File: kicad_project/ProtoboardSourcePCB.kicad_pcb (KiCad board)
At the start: 2 copper layers, 53 x 62.9 mm, 10 parts, among them J1 Conn_02x05_Odd_Even, J2 Conn_02x05_Odd_Even

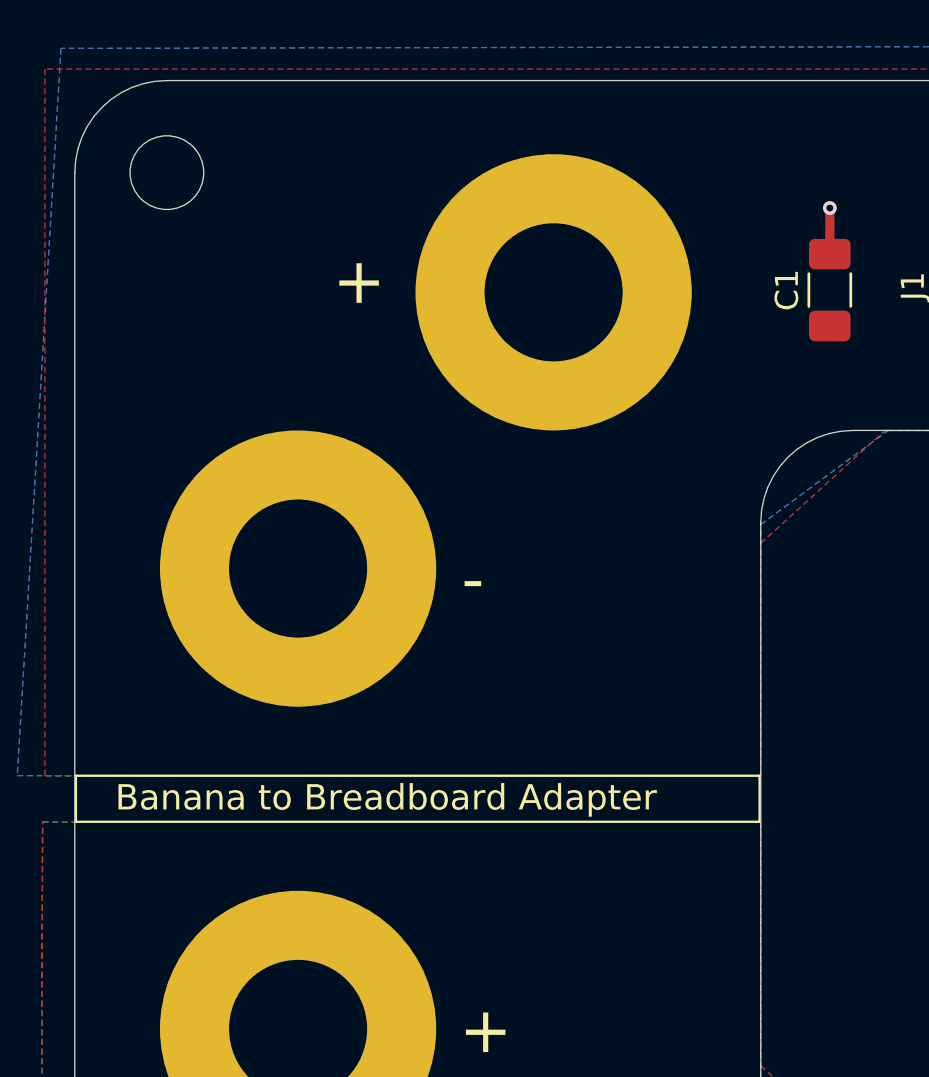
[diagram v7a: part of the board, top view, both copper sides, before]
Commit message: Agregando ultimos detalles y logo en el Silkscreen
Signed-off-by: RoMadrigal <rmadrigalmontes@gmail.com>
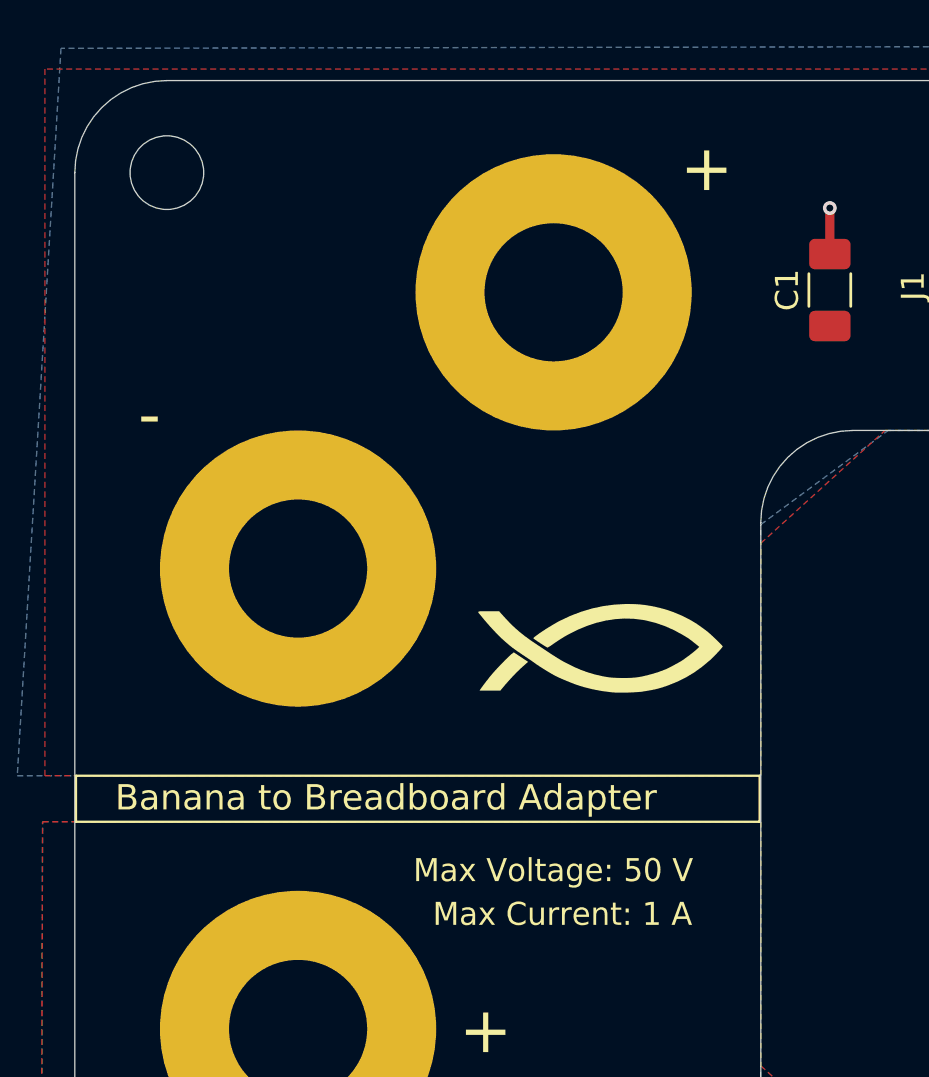
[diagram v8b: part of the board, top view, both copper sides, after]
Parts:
- added G***: LOGO, Logos:fish1, F.Cu at (133.0, 64.5)
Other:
- board text added: "Designed by: Rodrigo Madrigal Montes"
- board text added: "Max Current: 1 A"
- board text added: "Max Voltage: 50 V"
- board text removed: "Designed By: Rodrigo Madrigal Montes"
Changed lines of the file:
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@@
 	(net 3 "VDD")
 	(net 4 "GND2")
+	(footprint "Logos:fish1"
+		(layer "F.Cu")
+		(at 133 64.5)
+		(property "Reference" "G***"
+			(at 0 0 0)
+			(layer "F.SilkS")
+			(hide yes)
+			(effects
+				(font
+					(size 1.5 1.5)
+					(thickness 0.3)
+				)
+			)
+		)
+		(property "Value" "LOGO"
+			(at 0.75 0 0)
+			(layer "F.SilkS")
+			(hide yes)
+			(effects
+				(font
+					(size 1.5 1.5)
+					(thickness 0.3)
+				)
+			)
+		)
+		(property "Datasheet" ""
+			(at 0 0 0)
+			(layer "F.Fab")
+			(hide yes)
+			(effects
+				(font
+					(size 1.27 1.27)
+					(thickness 0.15)
+				)
+			)
+		)
+		(property "Description" ""
+			(at 0 0 0)
+			(layer "F.Fab")
+			(hide yes)
+			(effects
+				(font
+					(size 1.27 1.27)
+					(thickness 0.15)
+				)
+			)
+		)
+		(attr board_only exclude_from_pos_files exclude_from_bom)
+		(fp_poly
+			(pts
+				(xy -3.416751 0.347141) (xy -3.104273 0.554192) (xy -3.199105 0.633621) (xy -3.410967 0.821179)
+				(xy -3.633032 1.036653) (xy -3.858711 1.273265) (xy -4.081419 1.524236) (xy -4.189354 1.652689)
+				(xy -4.312394 1.801896) (xy -4.764901 1.801896) (xy -5.217408 1.801896) (xy -5.183151 1.748899)
+				(xy -5.132417 1.674759) (xy -5.06204 1.578084) (xy -4.977283 1.465756) (xy -4.883411 1.344657) (xy -4.785684 1.221668)
+				(xy -4.693054 1.108118) (xy -4.622083 1.025336) (xy -4.534365 0.927619) (xy -4.434648 0.819836)
+				(xy -4.327681 0.706856) (xy -4.218213 0.593549) (xy -4.110994 0.484784) (xy -4.010772 0.38543) (xy -3.922296 0.300357)
+				(xy -3.850316 0.234434) (xy -3.801413 0.193886) (xy -3.729229 0.14009)
+			)
+			(stroke
+				(width 0)
+				(type solid)
+			)
+			(fill yes)
+			(layer "F.SilkS")
+		)
+		(fp_poly
+			(pts
+				(xy 1.483303 -1.957004) (xy 1.731568 -1.942899) (xy 1.971119 -1.917313) (xy 2.214168 -1.878765)
+				(xy 2.472925 -1.825772) (xy 2.62814 -1.789502) (xy 2.947232 -1.699239) (xy 3.271495 -1.583108) (xy 3.591974 -1.445235)
+				(xy 3.899714 -1.289744) (xy 4.18576 -1.120761) (xy 4.400308 -0.973197) (xy 4.482943 -0.911861) (xy 4.574456 -0.843851)
+				(xy 4.65242 -0.785834) (xy 4.703224 -0.745084) (xy 4.770358 -0.687013) (xy 4.849201 -0.616058) (xy 4.93513 -0.536654)
+				(xy 5.023523 -0.453238) (xy 5.109757 -0.370247) (xy 5.189211 -0.292117) (xy 5.257261 -0.223283)
+				(xy 5.309286 -0.168183) (xy 5.340663 -0.131253) (xy 5.347875 -0.118368) (xy 5.334741 -0.092346)
+				(xy 5.298281 -0.044305) (xy 5.242906 0.021012) (xy 5.173027 0.098861) (xy 5.093055 0.1845) (xy 5.007401 0.273186)
+				(xy 4.920478 0.360174) (xy 4.836695 0.440723) (xy 4.776984 0.495474) (xy 4.444986 0.772471) (xy 4.107042 1.014674)
+				(xy 3.756826 1.225761) (xy 3.388009 1.409411) (xy 2.994261 1.569303) (xy 2.831818 1.626271) (xy 2.687166 1.672965)
+				(xy 2.550365 1.712411) (xy 2.412247 1.746695) (xy 2.263642 1.777904) (xy 2.095382 1.808123) (xy 1.898299 1.839439)
+				(xy 1.888618 1.840905) (xy 1.758321 1.856758) (xy 1.599572 1.869969) (xy 1.421535 1.880295) (xy 1.233372 1.887493)
+				(xy 1.044246 1.891316) (xy 0.863322 1.891522) (xy 0.699762 1.887866) (xy 0.562729 1.880104) (xy 0.529969 1.877122)
+				(xy 0.108151 1.822503) (xy -0.30112 1.745753) (xy -0.690215 1.6485) (xy -1.002125 1.549972) (xy -1.112419 1.509466)
+				(xy -1.243984 1.458203) (xy -1.387503 1.400087) (xy -1.533657 1.33902) (xy -1.67313 1.278904) (xy -1.796603 1.223644)
+				(xy -1.894759 1.177141) (xy -1.907892 1.170573) (xy -1.994925 1.123975) (xy -2.105421 1.060902)
+				(xy -2.230957 0.986533) (xy -2.363111 0.906046) (xy -2.493461 0.824622) (xy -2.613585 0.74744) (xy -2.71506 0.67968)
+				(xy -2.775115 0.637238) (xy -2.85329 0.581035) (xy -2.953241 0.511073) (xy -3.064443 0.434621) (xy -3.176368 0.358947)
+				(xy -3.227998 0.324544) (xy -3.402487 0.208179) (xy -3.550218 0.107616) (xy -3.677153 0.01829) (xy -3.789253 -0.06437)
+				(xy -3.892481 -0.144931) (xy -3.992797 -0.227962) (xy -4.096164 -0.31803) (xy -4.208544 -0.419704)
+				(xy -4.254558 -0.462062) (xy -4.363872 -0.567138) (xy -4.489643 -0.694826) (xy -4.62467 -0.83731)
+				(xy -4.761748 -0.986775) (xy -4.893676 -1.135406) (xy -5.013251 -1.275387) (xy -5.085056 -1.36318)
+				(xy -5.143797 -1.435812) (xy -5.194765 -1.49722) (xy -5.23271 -1.541189) (xy -5.252379 -1.561503)
+				(xy -5.252893 -1.561852) (xy -5.267907 -1.588241) (xy -5.27079 -1.610319) (xy -5.269218 -1.622191)
+				(xy -5.261441 -1.631246) (xy -5.242871 -1.637863) (xy -5.208916 -1.642424) (xy -5.154986 -1.64531)
+				(xy -5.076493 -1.646901) (xy -4.968845 -1.647579) (xy -4.827452 -1.647724) (xy -4.820149 -1.647725)
+				(xy -4.369509 -1.647725) (xy -4.296787 -1.56582) (xy -4.10984 -1.358811) (xy -3.936868 -1.17572)
+				(xy -3.771609 -1.011147) (xy -3.607807 -0.859692) (xy -3.439202 -0.715955) (xy -3.259537 -0.574533)
+				(xy -3.062551 -0.430027) (xy -2.841987 -0.277036) (xy -2.669121 -0.16128) (xy -2.471887 -0.030745)
+				(xy -2.303429 0.080565) (xy -2.160406 0.174738) (xy -2.039477 0.253863) (xy -1.937305 0.320027)
+				(xy -1.850547 0.375318) (xy -1.775865 0.421825) (xy -1.709918 0.461634) (xy -1.649367 0.496834)
+				(xy -1.590872 0.529514) (xy -1.531093 0.561759) (xy -1.466689 0.59566) (xy -1.416465 0.621805) (xy -1.103174 0.776125)
+				(xy -0.804527 0.904776) (xy -0.510074 1.011344) (xy -0.209365 1.099413) (xy 0.108052 1.172571) (xy 0.289073 1.206958)
+				(xy 0.434748 1.227125) (xy 0.608396 1.241945) (xy 0.800356 1.251343) (xy 1.000965 1.255244) (xy 1.200562 1.253572)
+				(xy 1.389485 1.246252) (xy 1.55807 1.233207) (xy 1.67663 1.217815) (xy 1.879328 1.179094) (xy 2.096623 1.128054)
+				(xy 2.317933 1.06777) (xy 2.532675 1.001322) (xy 2.730267 0.931785) (xy 2.900126 0.862239) (xy 2.901611 0.861571)
+				(xy 2.977024 0.825559) (xy 3.075834 0.775476) (xy 3.188119 0.71663) (xy 3.303962 0.654331) (xy 3.413441 0.593889)
+				(xy 3.506637 0.540612) (xy 3.551792 0.513568) (xy 3.627663 0.463684) (xy 3.724195 0.395586) (xy 3.832602 0.315932)
+				(xy 3.9441 0.23138) (xy 4.049907 0.148589) (xy 4.141237 0.074217) (xy 4.207814 0.016301) (xy 4.330045 -0.096359)
+				(xy 4.149999 -0.24125) (xy 4.049329 -0.321831) (xy 3.969339 -0.384282) (xy 3.900953 -0.434973) (xy 3.835096 -0.480273)
+				(xy 3.762692 -0.526553) (xy 3.674665 -0.580182) (xy 3.623064 -0.611081) (xy 3.231717 -0.824698)
+				(xy 2.83583 -1.00059) (xy 2.433456 -1.139488) (xy 2.022653 -1.242123) (xy 1.865731 -1.271462) (xy 1.479045 -1.31809)
+				(xy 1.083523 -1.328462) (xy 0.682023 -1.303048) (xy 0.277401 -1.242319) (xy -0.127485 -1.146745)
+				(xy -0.52978 -1.016797) (xy -0.926625 -0.852946) (xy -1.05994 -0.789529) (xy -1.253947 -0.691915)
+				(xy -1.423161 -0.601474) (xy -1.578784 -0.511593) (xy -1.732018 -0.415661) (xy -1.894064 -0.307067)
+				(xy -1.987168 -0.242247) (xy -2.07403 -0.182361) (xy -2.151345 -0.131316) (xy -2.213036 -0.092952)
+				(xy -2.253026 -0.071105) (xy -2.263809 -0.067514) (xy -2.28766 -0.07757) (xy -2.336301 -0.105089)
+				(xy -2.403576 -0.146031) (xy -2.483329 -0.196356) (xy -2.569405 -0.252026) (xy -2.655646 -0.309001)
+				(xy -2.735898 -0.363243) (xy -2.804005 -0.410711) (xy -2.853809 -0.447367) (xy -2.879155 -0.469172)
+				(xy -2.881109 -0.472543) (xy -2.865183 -0.495996) (xy -2.820233 -0.536127) (xy -2.750502 -0.590149)
+				(xy -2.660231 -0.655271) (xy -2.553661 -0.728705) (xy -2.435035 -0.807663) (xy -2.308594 -0.889355)
+				(xy -2.178581 -0.970992) (xy -2.049237 -1.049786) (xy -1.924803 -1.122947) (xy -1.809523 -1.187687)
+				(xy -1.726507 -1.23166) (xy -1.262455 -1.448634) (xy -0.793349 -1.6274) (xy -0.319166 -1.767963)
+				(xy 0.160115 -1.87033) (xy 0.644517 -1.934505) (xy 1.134061 -1.960494) (xy 1.214111 -1.961111)
+			)
+			(stroke
+				(width 0)
+				(type solid)
+			)
+			(fill yes)
+			(layer "F.SilkS")
+		)
+		(embedded_fonts no)
+	)
 	(footprint "MountingHole:MountingHole_3.2mm_M3"
 		(layer "F.Cu")
@@
 		)
 	)
+	(gr_text "Max Current: 1 A"
+		(at 125.75 76.6 0)
+		(layer "F.SilkS")
+		(effects
+			(font
+				(size 1 0.97)
+				(thickness 0.15)
+			)
+			(justify left bottom)
+		)
+	)
 	(gr_text "-"
 		(at 152.7 99 0)
@@
 		)
 	)
+	(gr_text "Max Voltage: 50 V"
+		(at 124.9 74.7 0)
+		(layer "F.SilkS")
+		(effects
+			(font
+				(size 1 0.97)
+				(thickness 0.15)
+			)
+			(justify left bottom)
+		)
+	)
 	(gr_text "-"
 		(at 157.8 99 0)
@@
 	)
 	(gr_text "+"
-		(at 121.4 49.7 0)
+		(at 136.5 44.8 0)
 		(layer "F.SilkS")
 		(effects
@@
 	)
 	(gr_text "-"
-		(at 127 62.65 0)
+		(at 112.95 55.5 0)
 		(layer "F.SilkS")
 		(effects
@@
 		)
 	)
-	(gr_text "Designed By: Rodrigo Madrigal Montes"
+	(gr_text "Designed by: Rodrigo Madrigal Montes"
 		(at 136.2 86.15 270)
 		(layer "B.SilkS")
